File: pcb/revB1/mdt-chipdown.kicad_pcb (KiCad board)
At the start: 4 copper layers, 94 x 79.6 mm, 137 parts, among them J1 BI, J2 BI, J3 SPDIF OUT, J4 Micro_SD_Card, J5 Micro_SD_Card, Q1 DMG2305UX, SW1 ON_OFF, SW2 PROGRAM, U1 TPD3S014, U10 TLV75733PDBV, U11 74LVC2G06, U2 AMS1117-3.3, U3 ILI9341 3.2" capacitive touch, U4 PCM5102A, U5 APS6404L-3SQR, U6 APS6404L-3SQR, U7 MKL02Z32VFG4, U8 GD25Q64ESIGR, U9 MIMXRT1062DVJ6B, Y1 24MHz, Y2 32768

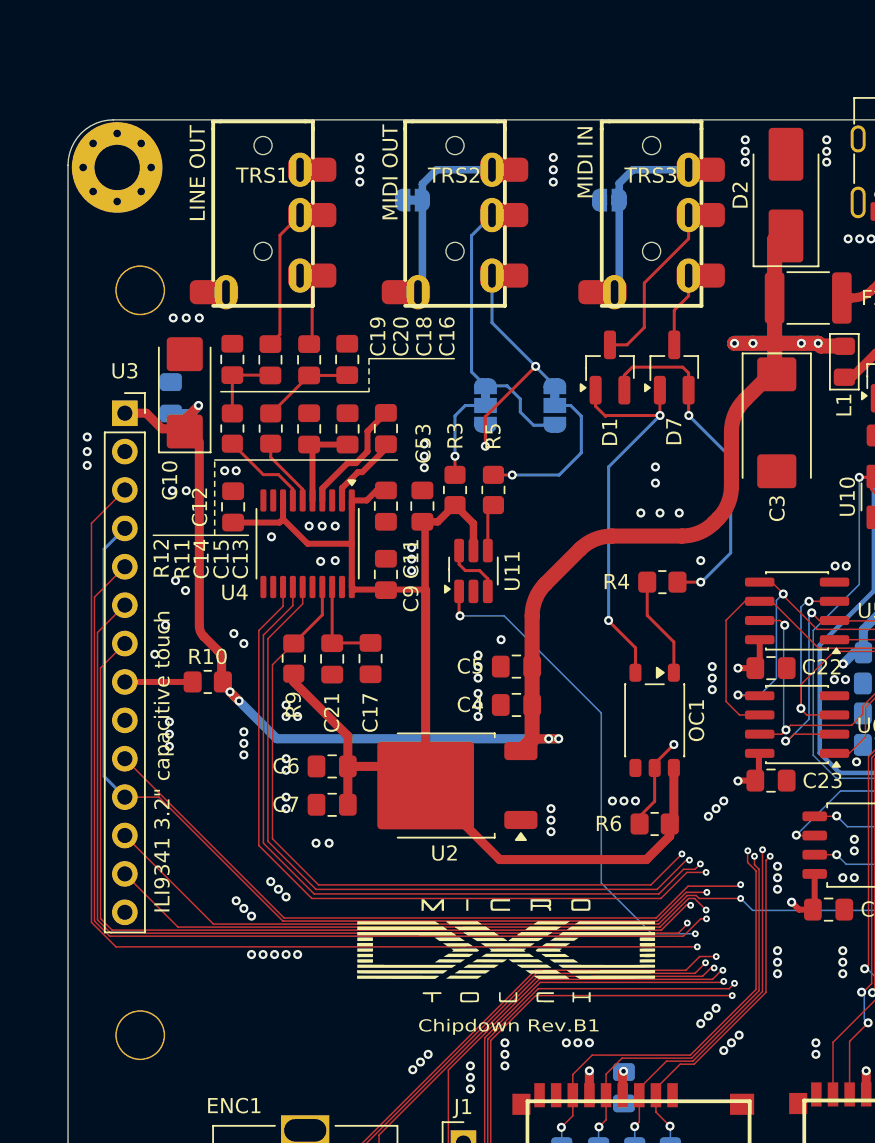
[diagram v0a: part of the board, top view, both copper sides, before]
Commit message: Added AGND
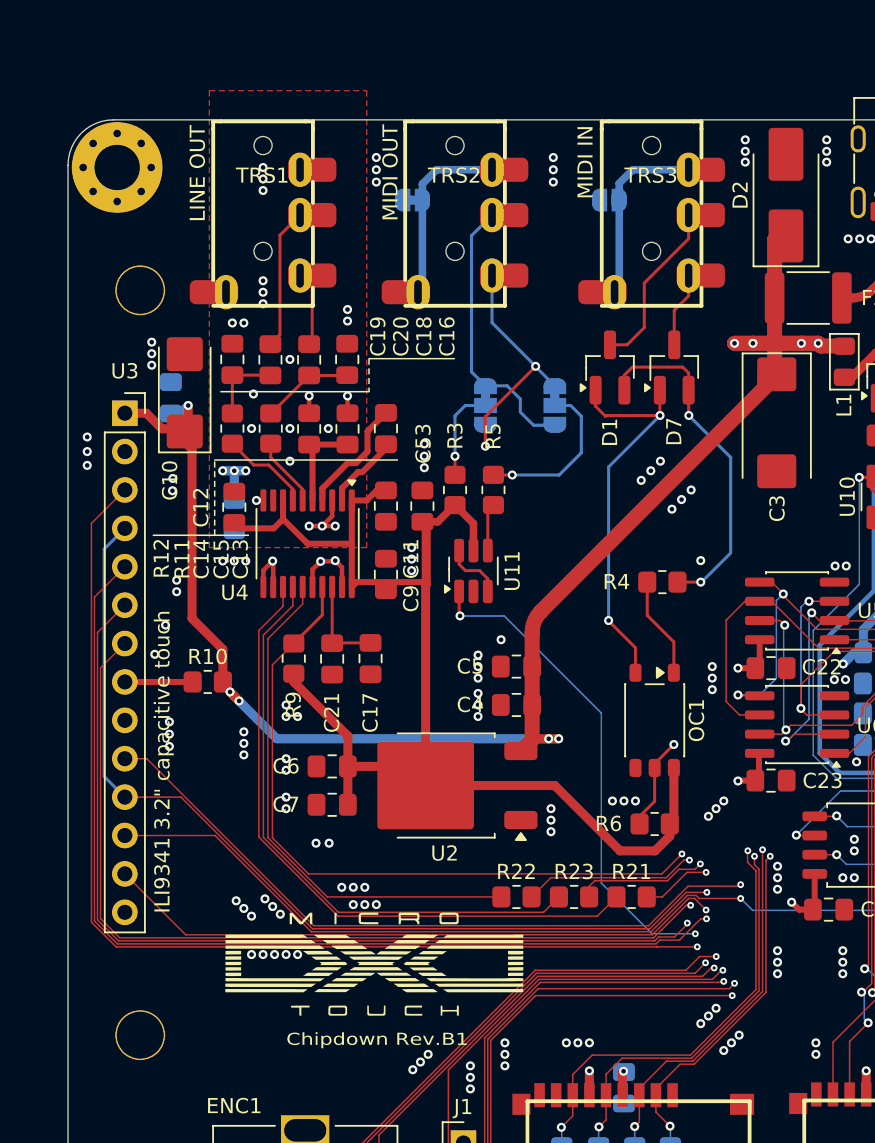
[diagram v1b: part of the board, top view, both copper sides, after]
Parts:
- added R21: 47, Resistor_SMD:R_0805_2012Metric_Pad1.20x1.40mm_HandSolder, F.Cu at (85.3, 85.3)
- added R22: 47, Resistor_SMD:R_0805_2012Metric_Pad1.20x1.40mm_HandSolder, F.Cu at (77.7, 85.3)
- added R23: 47, Resistor_SMD:R_0805_2012Metric_Pad1.20x1.40mm_HandSolder, F.Cu at (81.5, 85.3)
- added R24: 0, Resistor_SMD:R_0805_2012Metric_Pad1.20x1.40mm_HandSolder, B.Cu at (59.1, 60.1)
- moved LOGO1 8.76 mm to (68.3, 89.9)
- moved C12 0.08 mm to (59.1, 59.6)
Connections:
- C12 pad 1: GND -> AGND
- C16 pad 1: GND -> AGND
- C19 pad 1: GND -> AGND
- TRS1 pad R2: GND -> AGND
- TRS1 pad S: GND -> AGND
- U4 pad 9: GND -> AGND
- U9 pad B11: I2S_DATA -> Net-(U9GPIO-GPIO_B1_01)
- U9 pad J13: I2S_BCLK -> Net-(U9GPIO-GPIO_AD_B1_11)
- U9 pad L13: I2S_LRCK -> Net-(U9GPIO-GPIO_AD_B1_10)
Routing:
- net I2S_LRCK: track 94.1 -> 34.6 mm, vias 3 -> 0
- net Net-(U9GPIO-GPIO_AD_B1_10): track 0.00 -> 57.8 mm, vias 0 -> 3
- net I2S_BCLK: track 96.7 -> 43.6 mm, vias 3 -> 0
- net Net-(U9GPIO-GPIO_AD_B1_11): track 0.00 -> 51.8 mm, vias 0 -> 3
- net I2S_DATA: track 80.9 -> 39.4 mm, vias 2 -> 0
- net Net-(U9GPIO-GPIO_B1_01): track 0.00 -> 40.7 mm, vias 0 -> 2
- net GND: track 40.1 -> 58.6 mm, vias 250 -> 259
- net VCC: track 126.6 -> 122.8 mm
- net AGND: track 0.00 -> 3.45 mm, vias 0 -> 19
- net ~{MUTE}: track 90.6 -> 89.9 mm
- added copper zone on F.Cu, net AGND
- added copper zone on In1.Cu, net AGND
- added copper zone on In2.Cu, net AGND
